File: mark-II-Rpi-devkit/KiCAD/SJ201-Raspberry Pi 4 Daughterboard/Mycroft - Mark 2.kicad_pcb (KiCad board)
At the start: 4 copper layers, 72 x 93 mm, 210 parts, among them J1 Barrel_Jack, J10 Debug Connector, J11 I2S, J2 PVDD Jumper, J3 SPKLEFT, J4 SPKRIGHT, J5 PowerTP, J6 Raspberry_Pi_4, J7 USB_B_Micro, J8 MIC, J9 AudioJack3_Ground_Switch, P1 LED, P2 LED, P3 LED, P4 LED, Q3 AO3415A, Q4 FDV301N, SW1 MuteMic, U1 XL4501E1, U10 SPK0838HT4H-1, U11 SPK0838HT4H-1, U12 NCP303LSN30, U13 CM108B, U3 MAX9744, U4 AZ1117CH-3.3, U5 SN74LVC125APWR, U6 FE1.1s, U7 MP2359, U8 XMOS-XVF3510, U9 AT25SF161 16MBIT, X1 SG-210STF 24M, Y2 12MHz

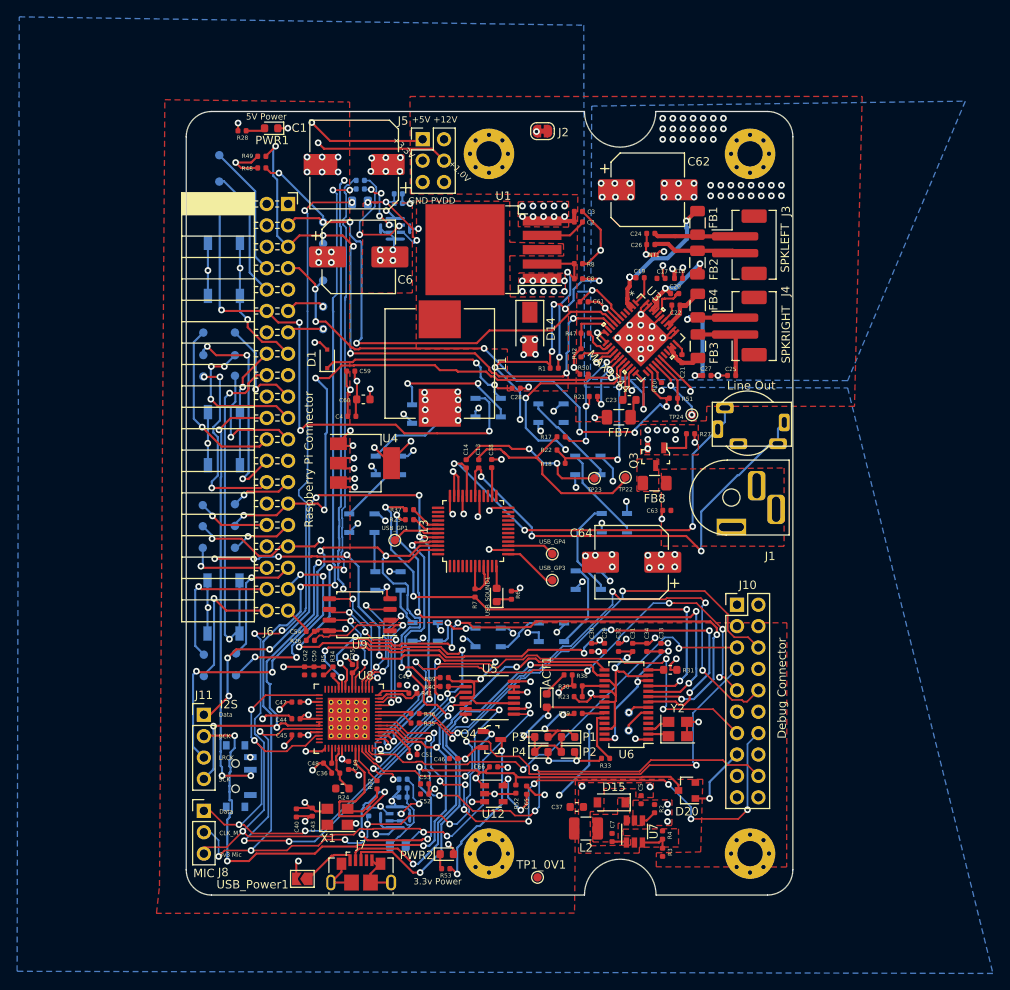
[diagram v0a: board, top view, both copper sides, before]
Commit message: Update to v0.66 - printed at JLC - 2nd spin
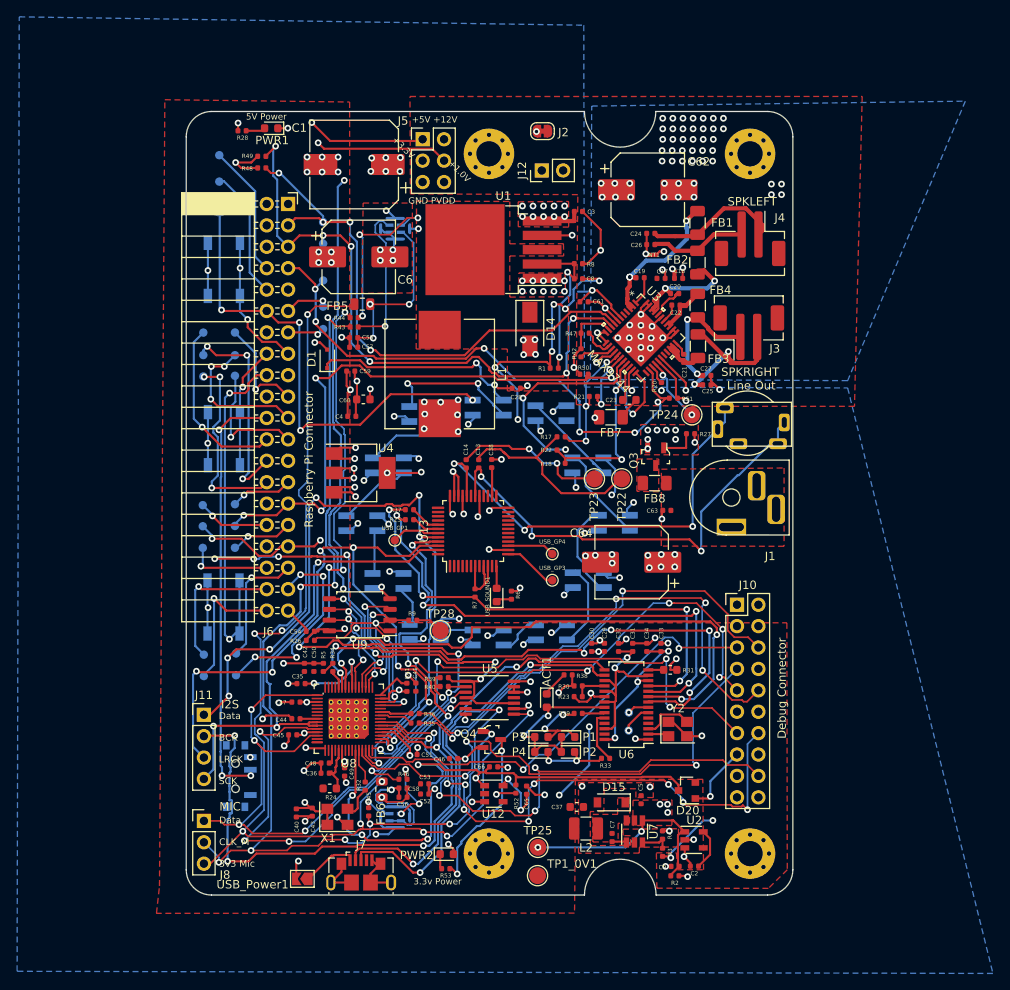
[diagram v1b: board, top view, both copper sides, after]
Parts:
- added C9: 1NF, Capacitor_SMD:C_0402_1005Metric, F.Cu at (58.0, 89.6)
- added J12: GND, Connector_PinHeader_2.54mm:PinHeader_1x02_P2.54mm_Vertical, F.Cu at (42.2, 7.00)
- added R9: 4.7k, Resistor_SMD:R_0402_1005Metric, F.Cu at (26.9, 60.4)
- added TP25: TestPoint, TestPoint:TestPoint_Pad_D2.0mm, F.Cu at (41.7, 87.3)
- added TP28: TestPoint, TestPoint:TestPoint_Pad_D2.0mm, F.Cu at (30.2, 61.6)
- added U2: NCP303LSN09, Package_TO_SOT_SMD:SOT-23-5, F.Cu at (60.3, 86.5)
- C2: value 1uF -> 2.2NF
- C55, C56, C57, C58, FB5, FB6, R43, R44, R45, R46: moved to F.Cu
- R2: value 100K -> 10k
- R28: value 330R -> 680R
- TP18, TP1_0V1, TP22, TP23, TP24: footprint TestPoint:TestPoint_Pad_D1.0mm -> TestPoint:TestPoint_Pad_D2.0mm
- U12: value NCP303LSN30 -> NCP303LSN09
- U8: footprint user:QFN-60-1EP_7x7mm_P0.4mm_EP5.6x5.6mm -> user:QFN-60-1EP_7x7mm_P0.4mm_EP5.6x5.6mm-HandSolder
- moved C2 77.7 mm to (60.3, 89.6), turned to 180 degrees
- moved C57 19.0 mm to (19.9, 28.0), turned to 180 degrees
- moved C55 16.8 mm to (19.9, 26.9), turned to 180 degrees
- moved R43 16.4 mm to (19.9, 25.6)
- moved R44 16.3 mm to (19.9, 24.5)
- moved FB5 12.1 mm to (20.9, 22.9)
- moved R2 8.33 mm to (58.0, 90.7), turned to 180 degrees
- moved FB6 6.89 mm to (23.2, 80.5), turned to 90 degrees
- moved C35 6.36 mm to (13.6, 67.9), turned to 180 degrees
- moved C25 3.15 mm to (61.8, 32.4), turned to 0 degrees
- moved C41 1.50 mm to (27.3, 68.3), turned to 90 degrees
- moved R24 1.50 mm to (17.0, 80.3)
- moved J3 1.46 mm to (66.9, 15.1), turned to 180 degrees
- moved R32 1.41 mm to (21.2, 80.1)
- moved J4 1.36 mm to (66.8, 26.3), turned to 0 degrees
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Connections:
- net Net-(R2-Pad2) renamed /Power/1v0Enable
- C2 pad 1: +12V -> Net-(C2-Pad1)
- C2 pad 2: Net-(C2-Pad2) -> GND
- R2 pad 1: +5V -> +3V3
- U1 pad 4: Net-(C2-Pad2) -> GND
- U12 pad 2: +3V3 -> +1V0
- X1 pad 1: Net-(X1-Pad1) -> +3V3
- Y2 pad 3: GND -> Net-(U6-Pad3)
- Y2 pad 4: Net-(U6-Pad3) -> GND
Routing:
- net /Power/1v0Enable: track 1.82 -> 26.3 mm, vias 0 -> 2
- net GND: track 237.6 -> 256.1 mm, vias 101 -> 105
- net /xmos/MIC_CLK_M: track 148.2 -> 130.3 mm, vias 10 -> 9
- net /xmos/MIC_DATA_M: track 108.0 -> 92.2 mm
- net Net-(R43-Pad2): track 6.63 -> 17.9 mm, vias 4 -> 1
- net Net-(C25-Pad1): track 9.24 -> 19.8 mm, vias 0 -> 2
- net RST_N: track 85.4 -> 76.9 mm
- net /xmos/3V3_MIC0: track 13.3 -> 21.7 mm
- net /xmos/3V3_MIC: track 142.0 -> 134.3 mm, vias 8 -> 9
- net +5V: track 97.0 -> 104.5 mm, vias 42 -> 41
- net +3V3: track 87.4 -> 94.7 mm, vias 23 -> 26
- net Net-(R44-Pad2): track 13.6 -> 20.8 mm, vias 2 -> 3
- net +1V0: track 30.7 -> 37.8 mm, vias 4 -> 5
- net Net-(C24-Pad1): track 9.67 -> 16.3 mm
- net GPIO18: track 63.4 -> 57.4 mm
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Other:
- board text added: "Mycroft MK2 v0.66 SJ201-01-02"
- board text removed: "Mycroft MK2 v0.65 SJ201-01-01"

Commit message: Fix missing items in schematic in Github
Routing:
- net Net-(C25-Pad1): track 19.8 -> 21.5 mm
- net Net-(C27-Pad2): track 15.3 -> 15.9 mm
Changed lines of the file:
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@@
     (thickness 1.6)
     (drawings 1914)
-    (tracks 2851)
+    (tracks 2852)
     (zones 0)
     (modules 216)
@@
     (0 F.Cu signal)
     (1 In1.Cu power hide)
-    (2 In2.Cu power)
+    (2 In2.Cu power hide)
     (31 B.Cu signal)
     (32 B.Adhes user hide)
     (33 F.Adhes user hide)
-    (34 B.Paste user)
-    (35 F.Paste user hide)
+    (34 B.Paste user hide)
+    (35 F.Paste user)
     (36 B.SilkS user hide)
     (37 F.SilkS user)
-    (38 B.Mask user)
-    (39 F.Mask user hide)
+    (38 B.Mask user hide)
+    (39 F.Mask user)
     (40 Dwgs.User user hide)
     (41 Cmts.User user hide)
@@
     (46 B.CrtYd user hide)
     (47 F.CrtYd user)
-    (48 B.Fab user)
-    (49 F.Fab user hide)
+    (48 B.Fab user hide)
+    (49 F.Fab user)
   )
   (setup
@@
   (segment (start 64.97657 29.85345) (end 64.3509 29.22778) (width 0.5) (layer F.Cu) (net 70))
   (segment (start 64.3509 29.22778) (end 64.3509 28.49118) (width 0.5) (layer F.Cu) (net 70))
-  (segment (start 64.3509 28.49118) (end 60.47232 32.36976) (width 0.5) (layer B.Cu) (net 70))
-  (via (at 60.33008 32.36976) (size 0.8) (drill 0.4) (layers F.Cu B.Cu) (net 70))
-  (segment (start 60.47232 32.36976) (end 60.33008 32.36976) (width 0.5) (layer B.Cu) (net 70))
-  (segment (start 60.40628 32.44596) (end 60.33008 32.36976) (width 0.5) (layer F.Cu) (net 70))
-  (segment (start 61.30304 32.44596) (end 60.40628 32.44596) (width 0.5) (layer F.Cu) (net 70))
+  (via (at 60.209899 32.554866) (size 0.8) (drill 0.4) (layers F.Cu B.Cu) (net 70))
+  (segment (start 64.3509 30.713957) (end 62.509991 32.554866) (width 0.5) (layer B.Cu) (net 70))
+  (segment (start 61.30304 32.44596) (end 61.194134 32.554866) (width 0.5) (layer F.Cu) (net 70))
+  (segment (start 64.3509 28.49118) (end 64.3509 30.713957) (width 0.5) (layer B.Cu) (net 70))
+  (segment (start 62.509991 32.554866) (end 60.209899 32.554866) (width 0.5) (layer B.Cu) (net 70))
+  (segment (start 61.194134 32.554866) (end 60.209899 32.554866) (width 0.5) (layer F.Cu) (net 70))
   (segment (start 55.694342 15.720158) (end 55.62078 15.79372) (width 0.5) (layer F.Cu) (net 71))
   (segment (start 57.196182 15.720158) (end 55.694342 15.720158) (width 0.5) (layer F.Cu) (net 71))
@@
   (segment (start 62.899724 26.75344) (end 65.76898 26.75344) (width 0.5) (layer F.Cu) (net 72))
   (segment (start 60.70854 24.44288) (end 61.95387 25.68821) (width 0.5) (layer F.Cu) (net 72))
-  (segment (start 59.47918 29.962892) (end 60.648846 31.132558) (width 0.5) (layer B.Cu) (net 72))
-  (segment (start 61.30558 31.33852) (end 60.854808 31.33852) (width 0.5) (layer F.Cu) (net 72))
-  (via (at 60.648846 31.132558) (size 0.8) (drill 0.4) (layers F.Cu B.Cu) (net 72))
-  (segment (start 60.854808 31.33852) (end 60.648846 31.132558) (width 0.5) (layer F.Cu) (net 72))
-  (segment (start 59.47918 24.68372) (end 59.47918 29.962892) (width 0.5) (layer B.Cu) (net 72))
+  (segment (start 61.30558 31.33852) (end 60.86148 31.33852) (width 0.5) (layer F.Cu) (net 72))
+  (via (at 60.6 31.6) (size 0.8) (drill 0.4) (layers F.Cu B.Cu) (net 72))
+  (segment (start 59.47918 24.68372) (end 60.6 25.80454) (width 0.5) (layer B.Cu) (net 72))
+  (segment (start 60.86148 31.33852) (end 60.6 31.6) (width 0.5) (layer F.Cu) (net 72))
+  (segment (start 60.6 25.80454) (end 60.6 31.6) (width 0.5) (layer B.Cu) (net 72))
   (via (at 34.43338 29.85453) (size 0.8) (drill 0.4) (layers F.Cu B.Cu) (net 73))
   (segment (start 34.94038 30.36153) (end 34.43338 29.85453) (width 0.25) (layer B.Cu) (net 73))

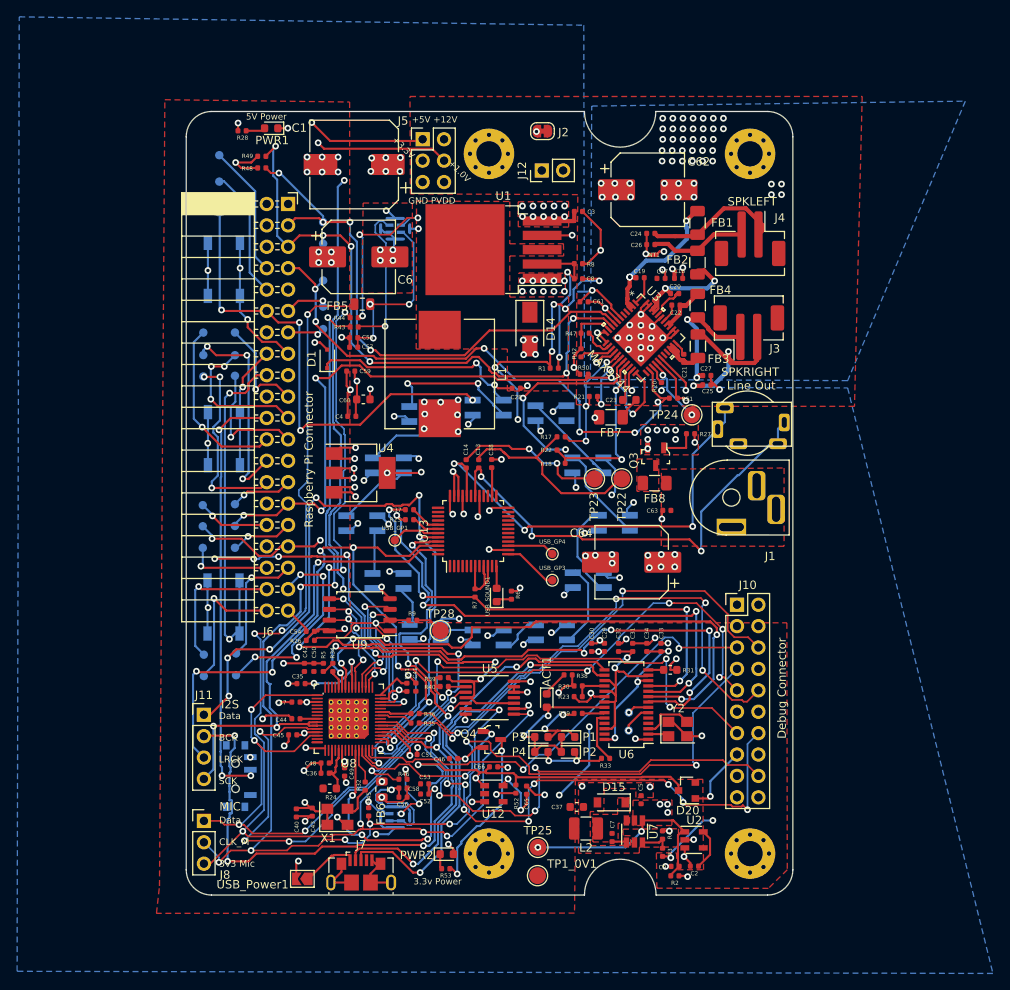
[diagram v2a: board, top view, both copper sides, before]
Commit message: SJ201 - Removed CM108b soundcard, added in I2S to Line out, ATTin402. Moved holes in layout. SJ202 - extened length to plug into USB2.0 port
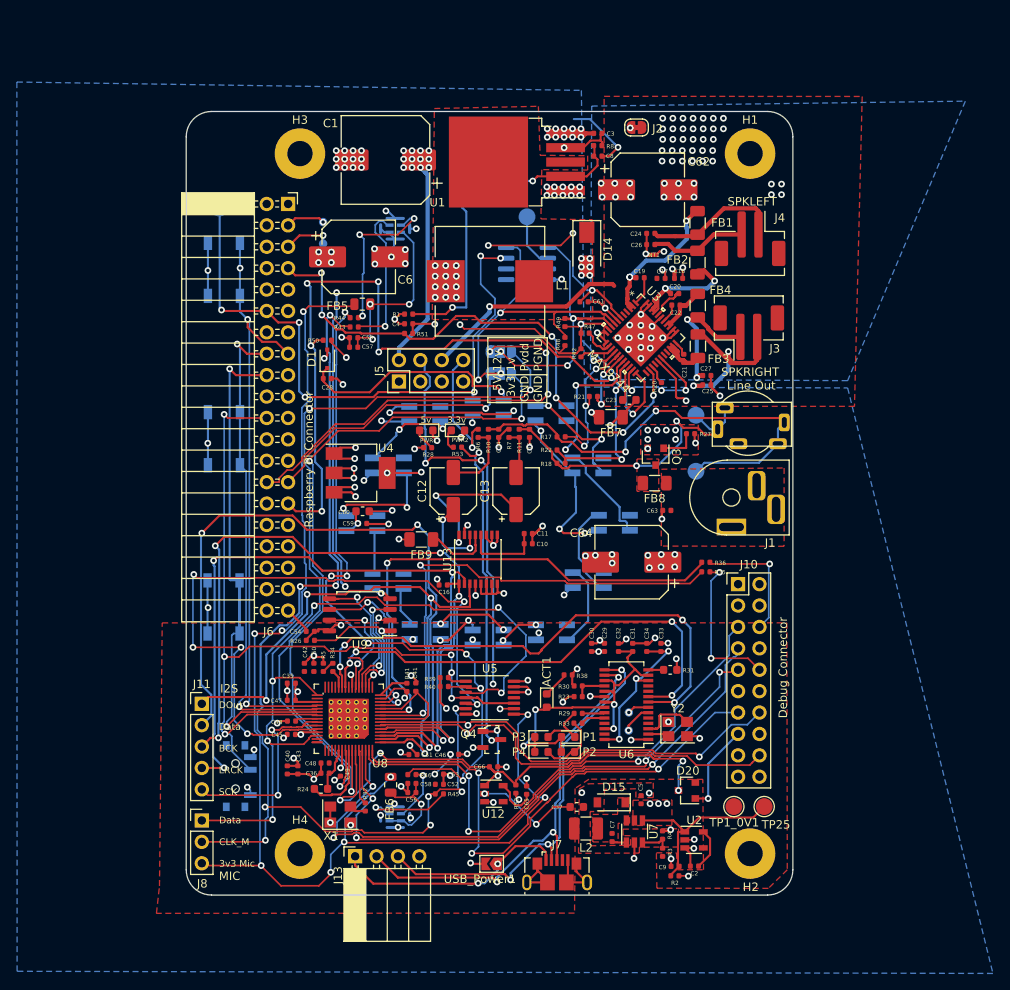
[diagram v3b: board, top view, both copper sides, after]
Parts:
- removed C38: 4.7UF, Capacitor_SMD:C_0402_1005Metric
- removed R25, R37: 22R, Resistor_SMD:R_0402_1005Metric
- removed R9: 4.7k, Resistor_SMD:R_0402_1005Metric
- removed TP0, TP1, TP10, TP11, TP12, TP13, TP14, TP15, TP16, TP17, TP19, TP20, TP21, TP26, TP27, TP4, TP5, TP6, TP7, TP8, TP9, USB_GP1, USB_GP3, USB_GP4: TestPoint, TestPoint:TestPoint_Pad_D1.0mm
- removed TP24, TP28: TestPoint, TestPoint:TestPoint_Pad_D2.0mm
- removed USB_SOUND1: LED, LED_SMD:LED_0603_1608Metric
- added C10: 100NF, Capacitor_SMD:C_0402_1005Metric, F.Cu at (40.6, 51.3)
- added C11: 10UF, Capacitor_SMD:C_0402_1005Metric, F.Cu at (40.6, 50.1)
- added C12: 47UF/16V, Capacitor_SMD:CP_Elec_5x5.3, F.Cu at (31.7, 45.0)
- added C15: 10nF, Capacitor_SMD:C_0402_1005Metric, F.Cu at (40.8, 38.2)
- added C16: 22pFDNP, Capacitor_SMD:C_0402_1005Metric, F.Cu at (30.5, 56.2)
- added FB9: FB, Resistor_SMD:R_1206_3216Metric, F.Cu at (27.9, 50.8)
- added J13: USB-PinHeader, Connector_PinSocket_2.54mm:PinSocket_1x04_P2.54mm_Horizontal, F.Cu at (20.1, 88.4)
- added J14: SDA, Jumper:SolderJumper-3_P1.3mm_Bridged2Bar12_RoundedPad1.0x1.5mm_NumberLabels, B.Cu at (37.4, 31.1)
- added Prog1: Prog, TestPoint:TestPoint_Pad_D2.0mm, B.Cu at (40.5, 12.5)
- added R10: 100R, Resistor_SMD:R_0402_1005Metric, F.Cu at (35.9, 38.2)
- added R11: 100R, Resistor_SMD:R_0402_1005Metric, F.Cu at (39.5, 38.2)
- added U14: ATtiny402-SS, Package_SO:SOIC-8_3.9x4.9mm_P1.27mm, B.Cu at (40.5, 18.1)
- C13: value 470pF -> 47UF/16V; footprint Capacitor_SMD:C_0402_1005Metric -> Capacitor_SMD:CP_Elec_5x5.3
- C14: value 470pF -> 10nF
- H1, H2, H3, H4: footprint MountingHole:MountingHole_3mm_Pad_Via -> MountingHole:MountingHole_3mm_Pad
- J11: footprint Connector_PinHeader_2.54mm:PinHeader_1x04_P2.54mm_Vertical -> Connector_PinHeader_2.54mm:PinHeader_1x05_P2.54mm_Vertical
- J12: value GND -> SCL; footprint Connector_PinHeader_2.54mm:PinHeader_1x02_P2.54mm_Vertical -> Jumper:SolderJumper-3_P1.3mm_Bridged2Bar12_RoundedPad1.0x1.5mm_NumberLabels; moved to B.Cu
- J5: footprint Connector_PinHeader_2.54mm:PinHeader_2x03_P2.54mm_Vertical -> Connector_PinHeader_2.54mm:PinHeader_2x04_P2.54mm_Vertical
- PWR1, PWR2: value LED -> LED_RED
- Q3: value AO3415A -> AO3401A; footprint digikey-footprints:SOT-23-3 -> Package_TO_SOT_SMD:SOT-23
- Q4: value FDV301N -> 2N7002
- R6: value 330R -> 220k
- R7: value 1k5 -> 220k
- TP22, TP23: moved to B.Cu
- U13: value CM108B -> UDA1334ATS; footprint Package_QFP:LQFP-48_7x7mm_P0.5mm -> Package_SO:SSOP-16_4.4x5.2mm_P0.65mm
- U4: value AZ1117CH-3.3 -> AMS1117-3.3
- moved PWR2 50.3 mm to (32.2, 37.9)
- moved R53 50.0 mm to (32.2, 39.9)
- moved R28 43.6 mm to (28.6, 39.9)
- moved R48 41.5 mm to (45.0, 27.3), turned to 90 degrees
- moved R49 41.0 mm to (45.0, 25.1), turned to 90 degrees
- moved PWR1 40.3 mm to (28.5, 37.9)
- moved R35 38.9 mm to (61.7, 54.6)
- moved R36 38.9 mm to (61.7, 53.5)
- moved R51 32.4 mm to (26.4, 26.4)
- moved R50 30.7 mm to (16.8, 27.1), turned to 180 degrees
- moved J5 28.9 mm to (25.2, 32.0), turned to 90 degrees
- moved TP25 27.3 mm to (68.6, 82.5)
- moved TP1_0V1 24.7 mm to (65.0, 82.5)
- moved J7 23.3 mm to (44.0, 90.3)
- moved USB_Power1 22.5 mm to (36.2, 89.3)
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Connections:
- net Net-(J7-Pad2) renamed /RaspberryPi/D-
- net Net-(J7-Pad3) renamed /RaspberryPi/D+
- C13 pad 1: VoutL -> Net-(C13-Pad1)
- C14 pad 1: VoutR -> PGND
- C14 pad 2: Net-(C14-Pad2) -> VoutL
- C23 pad 2: GNDA -> PGND
- FB7 pad 1: GNDA -> PGND
- J11 pad 1: I2S_DATA -> I2S_DOUT
- J11 pad 2: I2S_BCK -> I2S_DATA
- J11 pad 3: I2S_LRCK -> I2S_BCK
- J11 pad 4: I2S_SCK -> I2S_LRCK
- J12 pad 1: GND -> SCL_PI
- J12 pad 2: GND -> SCL
- J6 pad 27: Net-(J6-Pad27) -> SDA_PI
- J6 pad 28: Net-(J6-Pad28) -> SCL_PI
- J6 pad 3: SDA_PI -> Net-(J6-Pad3)
- J6 pad 5: SCL_PI -> Net-(J6-Pad5)
- R17 pad 1: Net-(C13-Pad2) -> VoutL
- R18 pad 1: Net-(C14-Pad2) -> VoutR
- R48 pad 2: SDA_PI -> SDA
- R49 pad 2: SCL_PI -> SCL
- R6 pad 1: GND -> Net-(C12-Pad2)
- R6 pad 2: Net-(R6-Pad2) -> PGND
- R7 pad 1: DREG33 -> Net-(C13-Pad2)
- R7 pad 2: USB_SOUNDCARD_D+ -> PGND
- TP2 pad 1: SDA_PI -> Net-(J6-Pad3)
- TP22 pad 1: Net-(C13-Pad2) -> VoutL
- TP23 pad 1: Net-(C14-Pad2) -> VoutR
- TP3 pad 1: SCL_PI -> Net-(J6-Pad5)
- U13 pad 1: Net-(U13-Pad1) -> I2S_BCK
- U13 pad 10: DREG33 -> GND
- U13 pad 11: Net-(U13-Pad11) -> GND
- U13 pad 14: GND -> Net-(C12-Pad1)
- U13 pad 15: Net-(U13-Pad15) -> PGND
- U13 pad 16: Net-(U13-Pad16) -> Net-(C13-Pad1)
- U13 pad 2: Net-(U13-Pad2) -> I2S_LRCK
- U13 pad 3: Net-(U13-Pad3) -> I2S_DOUT
- U13 pad 4: Net-(U13-Pad4) -> +3V3
- U13 pad 5: Net-(U13-Pad5) -> GND
- U13 pad 6: Net-(U13-Pad6) -> GND
- U13 pad 7: DREG33 -> GND
- U13 pad 8: Net-(U13-Pad8) -> GND
- U13 pad 9: DREG33 -> GND
- U3 pad 8: SDA_PI -> SDA
- U3 pad 9: SCL_PI -> SCL
- U6 pad 10: USB_SOUNDCARD_D- -> USB_MICRO_D-
- U6 pad 11: USB_SOUNDCARD_D+ -> USB_MICRO_D+
- U8 pad 30: TP1 -> Net-(U8-Pad30)
- U8 pad 34: INT_N -> GPIO22
- U8 pad 35: Net-(U8-Pad35) -> GPIO23
- U8 pad 36: Net-(U8-Pad36) -> GPIO24
- U8 pad 37: Net-(U8-Pad37) -> GPIO25
- U8 pad 45: TP2 -> TP1
- U8 pad 46: TP3 -> TP2
- U8 pad 47: TP4 -> TP3
- U8 pad 49: TP5 -> TP4
- U8 pad 52: I2C_SCL -> SCL_XMOS
- U8 pad 54: I2C_SDA -> SDA_XMOS
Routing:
- net SCL_XMOS: track 0.00 -> 88.9 mm, vias 0 -> 3
- net SDA_XMOS: track 0.00 -> 82.7 mm, vias 0 -> 3
- net I2S_DOUT: track 0.00 -> 71.7 mm, vias 0 -> 4
- net +5V: track 104.5 -> 39.3 mm, vias 41 -> 32
- net USB_SOUNDCARD_D-: track 61.0 -> 0.00 mm, vias 4 -> 0
- net USB_SOUNDCARD_D+: track 58.6 -> 0.00 mm, vias 4 -> 0
- net Net-(R36-Pad1): track 3.98 -> 61.7 mm, vias 0 -> 2
- net +1V0: track 37.8 -> 94.3 mm, vias 5 -> 7
- net GPIO22: track 16.9 -> 71.4 mm, vias 2 -> 3
- net Net-(R35-Pad1): track 4.27 -> 58.3 mm, vias 0 -> 2
- net +3V3: track 94.7 -> 138.9 mm, vias 26 -> 33
- net GPIO23: track 14.5 -> 57.2 mm, vias 1 -> 2
- net /xmos/XL_UP0: track 59.9 -> 18.1 mm, vias 4 -> 2
- net SDA: track 0.00 -> 40.2 mm, vias 0 -> 3
- net /xmos/XL_UP1: track 53.1 -> 15.2 mm, vias 2 -> 1
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- added copper zone on In2.Cu, net +3V3
- added copper zone on B.Cu, net +5V
- removed copper zone on B.Cu, net +3V3
- removed copper zone on In2.Cu, net +5V
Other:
- outline, holes or cut-outs redrawn
- board text added: "12v 1v Pvdd PGND"
- board text added: "3.3v"
- board text added: "5V 3v3 GND GND"
- board text added: "5v"
- board text added: "DOut Data BCK LRCK SCK"
- board text added: "I2C Selector XMOS I2C Raspi"
- board text added: "Mycroft MK2 v0.67 SJ201-01-03"
- board text removed: "+1.0V"
- board text removed: "+12V +5V"
- board text removed: "+3.3V"
- board text removed: "+5V +12V"
- board text removed: "3.3V+"
- board text removed: "3.3v Power"
- board text removed: "5V Power"
- board text removed: "Data BCK LRCK SCK"
- board text removed: "GND PVDD"
- board text removed: "Mycroft MK2 v0.66 SJ201-01-02"
- board text removed: "PVDD GND"
